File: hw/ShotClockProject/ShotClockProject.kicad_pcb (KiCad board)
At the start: 4 copper layers, 71.8 x 71.8 mm, 115 parts, among them IC1 TP4056-42-ESOP8_Rearanged, J1 USB4120-03-C_REVA, J2 Conn_ST_STDC14, J3 Conn_01x06_Pin, J4 SM03B-SRSS-TB(LF)(SN)(P), J5 Conn_01x02_Pin, J6 Conn_01x03_Pin, Q1 Q_NPN_BCE, Q2 Q_PMOS_SGD, Q3 Q_NPN_BCE, Q4 Q_NPN_BCE, SW1 TK-6580S-1, SW2 SW_SPDT, SW3 TK-6580S-2, SW4 TK-6580S-2, SW5 TK-6580S-2, U1 STM32F103RCT6, U2 LD39015M33R, U3 TPS63000, U4 TPS63000, U5 M74HC14YRM13TR, U6 USBLC6-2SC6, Y1 16MHz

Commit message: Finished routing
Added assembly holes
Added JLCJLCJLCJLC tag to hide their order number
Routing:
- net /Connectors to segment displays/DISP1_SEG_D: track 200.6 -> 244.8 mm, vias 5 -> 7
- net /Connectors to segment displays/DISP2_SEG_A: track 185.2 -> 226.8 mm, vias 5 -> 7
- net /Connectors to segment displays/DISP1_SEG_E: track 200.3 -> 240.1 mm, vias 5 -> 6
- net /Connectors to segment displays/DISP1_SEG_F: track 200.6 -> 239.9 mm, vias 5 -> 6
- net /Connectors to segment displays/DISP1_SEG_G: track 191.7 -> 227.1 mm, vias 7 -> 9
- net /Connectors to segment displays/DISP2_SEG_G: track 165.4 -> 192.3 mm, vias 5 -> 6
- net /Connectors to segment displays/DISP2_SEG_C: track 192.1 -> 218.3 mm, vias 7 -> 9
- net /Connectors to segment displays/DISP1_SEG_DP: track 198.9 -> 225.0 mm, vias 7 -> 9
- net /Connectors to segment displays/TIM2_CH1_PWM1_SEG: track 200.0 -> 224.8 mm, vias 7 -> 10
- net /Connectors to segment displays/DISP2_SEG_B: track 190.6 -> 215.3 mm, vias 5 -> 7
- net /Connectors to segment displays/DISP2_SEG_DP: track 144.6 -> 164.7 mm
- net /Connectors to segment displays/DISP2_SEG_F: track 174.3 -> 193.4 mm, vias 5 -> 6
- net /Connectors to segment displays/DISP2_SEG_E: track 173.3 -> 189.6 mm, vias 5 -> 6
- net GNDPWR: track 88.5 -> 92.1 mm
- net Net-(R1-Pad1): track 123.3 -> 121.9 mm
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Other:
- outline, holes or cut-outs redrawn
- board text added: "JLCJLCJLCJLC"

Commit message: Added LCSC Part number
Renamed output folders
Created first output files for REV1
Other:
- board text added: "REV 1"
- board text added: "Shot Clock Mainboard"
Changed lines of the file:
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@@
       (drillshape 0)
       (scaleselection 1)
-      (outputdirectory "output/mftr/gbr/v0.1/")
+      (outputdirectory "output/mftr/gerber/rev1/")
     )
   )
@@
     (fp_line (start 5.625 5) (end 4.625 5)
       (stroke (width 0.1) (type solid)) (layer "F.Fab"))
-    (pad "1" smd roundrect (at -7.65 -2.54 90) (size 4.6 1.1) (layers "F.Cu" "F.Paste" "F.Mask") (roundrect_rratio 0.227273)
+    (pad "1" smd roundrect (at -7.65 -2.54 90) (size 4.6 1.1) (layers "F.Cu" "F.Paste" "F.Mask") (roundrect_rratio 0.2272727273)
       (net 8 "+BATT") (pinfunction "S") (pintype "passive"))
-    (pad "2" smd roundrect (at -0.925 -2.775 90) (size 4.55 5.25) (layers "F.Cu" "F.Paste") (roundrect_rratio 0.054945)
+    (pad "2" smd roundrect (at -0.925 -2.775 90) (size 4.55 5.25) (layers "F.Cu" "F.Paste") (roundrect_rratio 0.05494505495)
       (net 90 "Net-(Q2-G)") (pinfunction "G") (pintype "input"))
-    (pad "2" smd roundrect (at -0.925 2.775 90) (size 4.55 5.25) (layers "F.Cu" "F.Paste") (roundrect_rratio 0.054945)
+    (pad "2" smd roundrect (at -0.925 2.775 90) (size 4.55 5.25) (layers "F.Cu" "F.Paste") (roundrect_rratio 0.05494505495)
       (net 90 "Net-(Q2-G)") (pinfunction "G") (pintype "input"))
-    (pad "2" smd roundrect (at 1.5 0 90) (size 9.4 10.8) (layers "F.Cu" "F.Mask") (roundrect_rratio 0.026596)
+    (pad "2" smd roundrect (at 1.5 0 90) (size 9.4 10.8) (layers "F.Cu" "F.Mask") (roundrect_rratio 0.02659595745)
       (net 90 "Net-(Q2-G)") (pinfunction "G") (pintype "input"))
-    (pad "2" smd roundrect (at 3.925 -2.775 90) (size 4.55 5.25) (layers "F.Cu" "F.Paste") (roundrect_rratio 0.054945)
+    (pad "2" smd roundrect (at 3.925 -2.775 90) (size 4.55 5.25) (layers "F.Cu" "F.Paste") (roundrect_rratio 0.05494505495)
       (net 90 "Net-(Q2-G)") (pinfunction "G") (pintype "input"))
-    (pad "2" smd roundrect (at 3.925 2.775 90) (size 4.55 5.25) (layers "F.Cu" "F.Paste") (roundrect_rratio 0.054945)
+    (pad "2" smd roundrect (at 3.925 2.775 90) (size 4.55 5.25) (layers "F.Cu" "F.Paste") (roundrect_rratio 0.05494505495)
       (net 90 "Net-(Q2-G)") (pinfunction "G") (pintype "input"))
-    (pad "3" smd roundrect (at -7.65 2.54 90) (size 4.6 1.1) (layers "F.Cu" "F.Paste" "F.Mask") (roundrect_rratio 0.227273)
+    (pad "3" smd roundrect (at -7.65 2.54 90) (size 4.6 1.1) (layers "F.Cu" "F.Paste" "F.Mask") (roundrect_rratio 0.2272727273)
       (net 44 "/Li-Po Battery and charger/charger_out") (pinfunction "D") (pintype "passive"))
     (model "${KICAD6_3DMODEL_DIR}/Package_TO_SOT_SMD.3dshapes/TO-263-2.wrl"
@@
     (property "Sheetname" "Connectors to segment displays")
     (attr smd)
-    (fp_text reference "FPC1" (at -7.75 3.25) (layer "F.SilkS")
+    (fp_text reference "FPC1" (at -9.6 -2 90) (layer "F.SilkS")
         (effects (font (size 1 1) (thickness 0.15)))
     )
@@
     (property "Sheetname" "STM32F103RCT6")
     (attr smd)
-    (fp_text reference "BUZZER1" (at 4.4 -5.4) (layer "F.SilkS")
+    (fp_text reference "BUZZER1" (at -6.2 1.2 90) (layer "F.SilkS")
         (effects (font (size 1 1) (thickness 0.15)))
     )
@@
   (gr_line (start 187 64.1) (end 121 64.1)
     (stroke (width 0.1) (type default)) (layer "Edge.Cuts"))
-  (gr_text "JLCJLCJLCJLC" (at 140 115.8) (layer "F.SilkS")
+  (gr_text "Shot \nClock \nMainboard" (at 123.8 135.2) (layer "F.SilkS")
+    (effects (font (size 1 1) (thickness 0.15)) (justify left bottom))
+  )
+  (gr_text "JLCJLCJLCJLC" (at 152.8 102) (layer "F.SilkS")
+    (effects (font (size 0.9 0.9) (thickness 0.15)) (justify left bottom))
+  )
+  (gr_text "REV 1" (at 120.4 129.8 90) (layer "F.SilkS")
     (effects (font (size 1 1) (thickness 0.15)) (justify left bottom))
   )

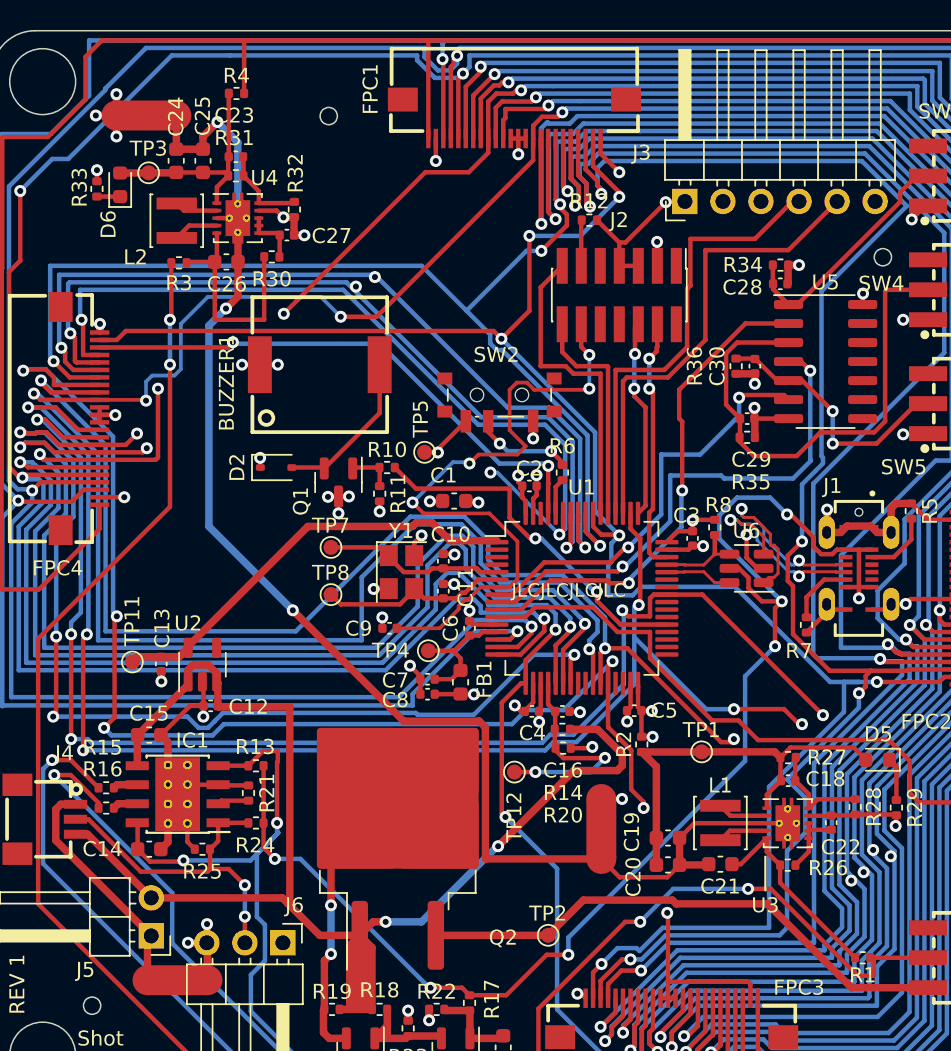
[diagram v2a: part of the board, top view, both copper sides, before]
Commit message: Added LCSC part numbers, and changed TPS vias
- Changed the footprint for the TPS regulators, so they don't have 0.2mm vias. Manually placed GND vias next to the footprint.
- Removed NETTIES to get rid of weird across the map connection of GND and GNDPWR.
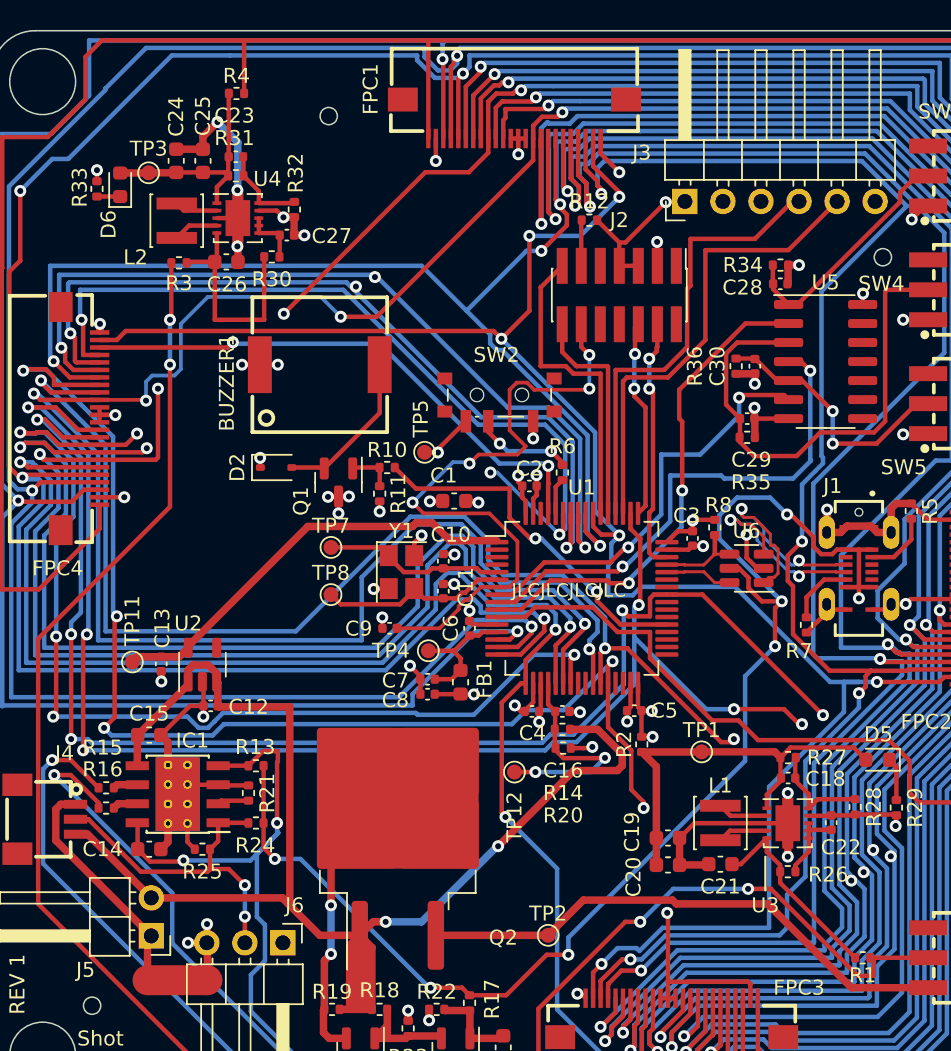
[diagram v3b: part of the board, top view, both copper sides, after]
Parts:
- removed NT2, NT3: NetTie_2, NetTie:NetTie-2_SMD_Pad2.0mm
- U3, U4: footprint Package_SON_Altered:Texas_DRC0010J_ThermalVias_Altered -> Package_SON:Texas_DRC0010J
- moved R26 0.44 mm to (171.2, 120.2)
- moved C18 0.17 mm to (171.3, 114.0)
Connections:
- C19 pad 2: GNDPWR -> GND
- C20 pad 2: GNDPWR -> GND
- C21 pad 2: GNDPWR -> GND
- C24 pad 2: GNDPWR -> GND
- C25 pad 2: GNDPWR -> GND
- C26 pad 2: GNDPWR -> GND
- U3 pad 11: GNDPWR -> GND
- U3 pad 3: GNDPWR -> GND
- U4 pad 11: GNDPWR -> GND
- U4 pad 3: GNDPWR -> GND
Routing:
- net GNDPWR: track 92.1 -> 0.00 mm, vias 3 -> 0
- net GND: track 161.9 -> 188.1 mm, vias 55 -> 56
- net /Connectors to segment displays/DISP2_SEG_B: track 215.3 -> 217.6 mm
- net /Connectors to segment displays/DISP2_SEG_DP: track 164.7 -> 163.7 mm

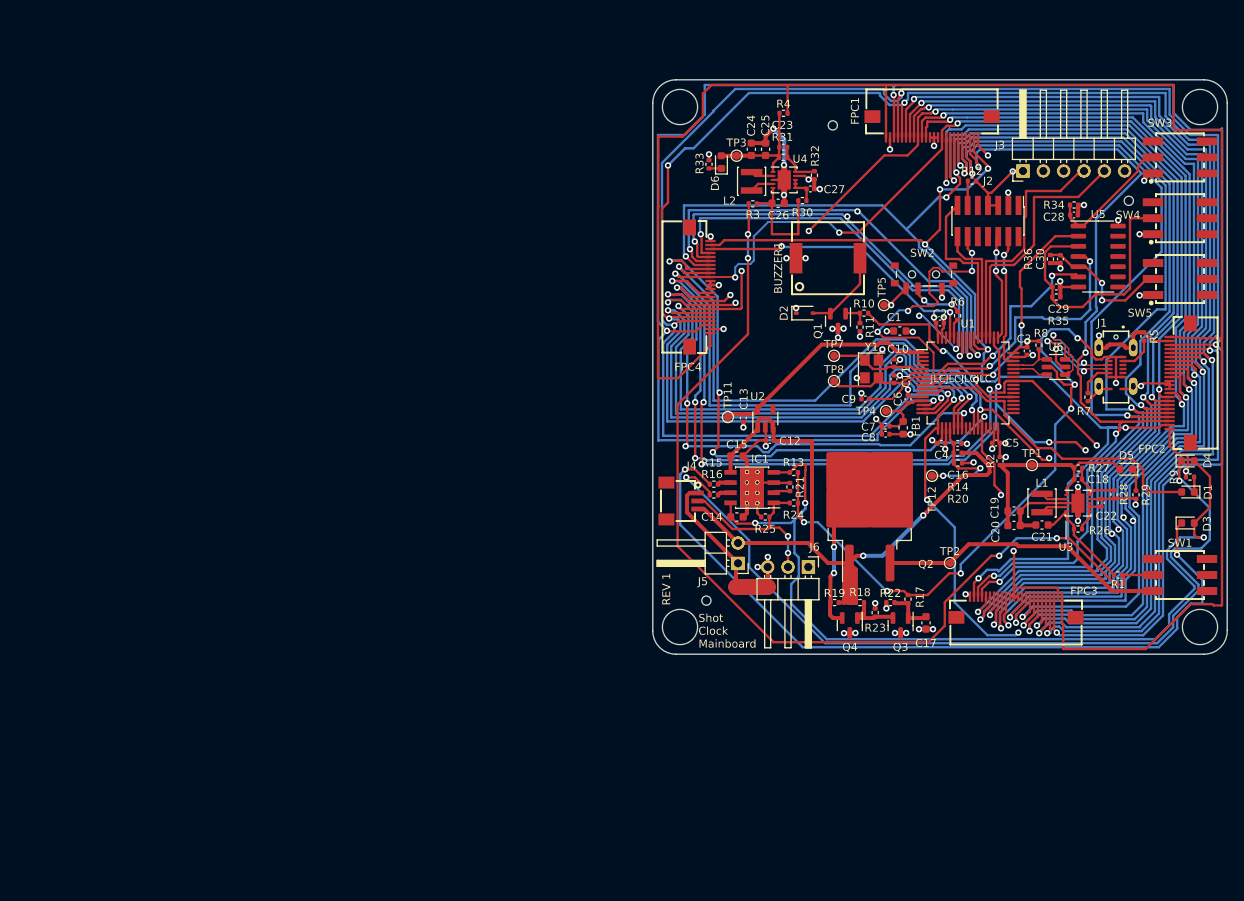
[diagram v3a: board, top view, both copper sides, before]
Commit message: Added I2C support
Calculated pull-up resistor values
Added 6 pin female headers to mainboard
Added nRESET line for the I2C chips
Removed PCB routing and part placement
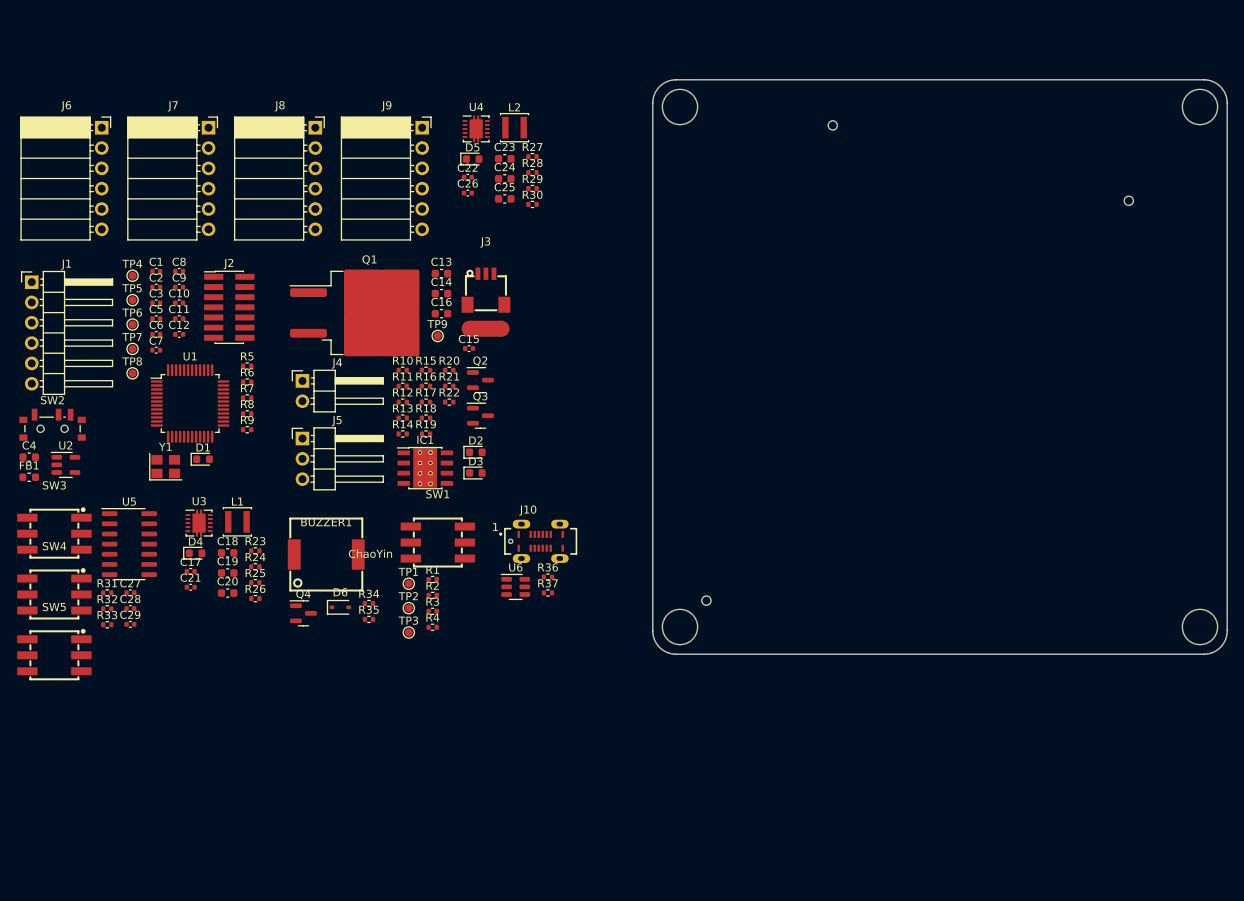
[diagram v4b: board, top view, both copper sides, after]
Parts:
- removed C30: 100n, Capacitor_SMD:C_0402_1005Metric
- removed FPC1, FPC2, FPC3, FPC4: AFC01-S24FCA-00, AFC01-S24FCA-00:FPC-SMD_P0.50-24P_FGS-XJ-H2.0
- removed TP11, TP12: TestPoint, TestPoint:TestPoint_Pad_D1.0mm
- added J10: USB4120-03-C_REVA, USB4120-03-C:GCT_USB4120-03-C_REVA_With3DModel, F.Cu at (104.1, 121.8)
- added J7: Conn_01x06_Pin, Connector_PinSocket_2.54mm:PinSocket_1x06_P2.54mm_Horizontal, F.Cu at (62.6, 70.1)
- added J8: Conn_01x06_Pin, Connector_PinSocket_2.54mm:PinSocket_1x06_P2.54mm_Horizontal, F.Cu at (75.9, 70.1)
- added J9: Conn_01x06_Pin, Connector_PinSocket_2.54mm:PinSocket_1x06_P2.54mm_Horizontal, F.Cu at (89.3, 70.1)
- added R37: 5k1, Resistor_SMD:R_0402_1005Metric, F.Cu at (105.0, 128.2)
- added TP6: TestPoint, TestPoint:TestPoint_Pad_D1.0mm, F.Cu at (53.1, 94.7)
- added TP9: TestPoint, TestPoint:TestPoint_Pad_D1.0mm, F.Cu at (91.2, 96.1)
- C1: value 10u -> 10n; footprint Capacitor_SMD:C_0603_1608Metric -> Capacitor_SMD:C_0402_1005Metric
- C10, C11: value 6p -> 100n
- C13: value 1u -> 10u; footprint Capacitor_SMD:C_0402_1005Metric -> Capacitor_SMD:C_0603_1608Metric
- C15: value 10u -> 100n; footprint Capacitor_SMD:C_0603_1608Metric -> Capacitor_SMD:C_0402_1005Metric
- C16: value 100n -> 10n; footprint Capacitor_SMD:C_0402_1005Metric -> Capacitor_SMD:C_0603_1608Metric
- C17: value 10n -> 2.2p; footprint Capacitor_SMD:C_0603_1608Metric -> Capacitor_SMD:C_0402_1005Metric
- C18, C23: value 2.2p -> 10u; footprint Capacitor_SMD:C_0402_1005Metric -> Capacitor_SMD:C_0603_1608Metric
- C2, C3, C9: value 100n -> 1u
- C21, C26: value 10u -> 0.1u; footprint Capacitor_SMD:C_0603_1608Metric -> Capacitor_SMD:C_0402_1005Metric
- C22: value 0.1u -> 2.2p
- C27: value 0.1u -> 100n
- C4: value 100n -> 4700n; footprint Capacitor_SMD:C_0402_1005Metric -> Capacitor_SMD:C_0603_1608Metric
- C6: value 10n -> 100n
- C7, C8: value 1u -> 6p
- D2: value 1N4148 -> G_LED; footprint Diode_SMD:D_SOD-323 -> LED_SMD:LED_0603_1608Metric
- D3: value G_LED -> R_LED
- D4: value R_LED -> G_LED
- D6: value G_LED -> 1N4148; footprint LED_SMD:LED_0603_1608Metric -> Diode_SMD:D_SOD-323
- J1: value USB4120-03-C_REVA -> Conn_01x06_Pin; footprint USB4120-03-C:GCT_USB4120-03-C_REVA_With3DModel -> Connector_PinHeader_2.54mm:PinHeader_1x06_P2.54mm_Horizontal
- J3: value Conn_01x06_Pin -> SM03B-SRSS-TB(LF)(SN)(P); footprint Connector_PinHeader_2.54mm:PinHeader_1x06_P2.54mm_Horizontal -> SM03B-SRSS-TB:CONN-SMD_SM03B-SRSS-TB-LF-SN-P
- J4: value SM03B-SRSS-TB(LF)(SN)(P) -> Conn_01x02_Pin; footprint SM03B-SRSS-TB:CONN-SMD_SM03B-SRSS-TB-LF-SN-P -> Connector_PinHeader_2.54mm:PinHeader_1x02_P2.54mm_Horizontal
- J5: value Conn_01x02_Pin -> Conn_01x03_Pin; footprint Connector_PinHeader_2.54mm:PinHeader_1x02_P2.54mm_Horizontal -> Connector_PinHeader_2.54mm:PinHeader_1x03_P2.54mm_Horizontal
- J6: value Conn_01x03_Pin -> Conn_01x06_Pin; footprint Connector_PinHeader_2.54mm:PinHeader_1x03_P2.54mm_Horizontal -> Connector_PinSocket_2.54mm:PinSocket_1x06_P2.54mm_Horizontal
- Q1: value Q_NPN_BCE -> Q_PMOS_SGD; footprint Package_TO_SOT_SMD:SOT-23 -> Package_TO_SOT_SMD:TO-263-2
- Q2: value Q_PMOS_SGD -> Q_NPN_BCE; footprint Package_TO_SOT_SMD:TO-263-2 -> Package_TO_SOT_SMD:SOT-23
- R10: value 300R -> 0.4R
- R11, R16, R17: value 1k -> 100k
- R12: value 100R -> 1k
- R13: value 0.4R -> 1k
- R14: value 1M -> 1k
- R18: value 1k -> 1k2
- R19: value 100k -> 10k
- R20, R31: value 1M -> 10k
- R21: value 1k2 -> 4780R
- R22: value 10k -> 86k6
- R23: value 10k -> 100R
- R24: value 4780R -> 1M
- R25: value 86k6 -> 178k
- R26, R30: value 100R -> 1k5
- R27: value 1M -> 100R
- R28: value 178k -> 1M
- R29: value 1k5 -> 110k
- R32: value 110k -> 10k
- R33, R8: value 1k5 -> 10k
- R34: value 10k -> 300R
- R35: value 10k -> 1k
- R36: value 10k -> 5k1
- R5: value 5k1 -> 1.5k
- R6: value 10k -> 1.5k
- R7: value 5k1 -> 130R
- R9: value 130R -> 100R
- U1: value STM32F103RCT6 -> STM32G070CBTx; footprint Package_QFP:LQFP-64_10x10mm_P0.5mm -> Package_QFP:LQFP-48_7x7mm_P0.5mm
- moved SW3 148.4 mm to (43.3, 120.8), turned to 0 degrees
- moved SW4 148.4 mm to (43.3, 128.4), turned to 0 degrees
- moved SW5 148.4 mm to (43.3, 136.0), turned to 0 degrees
- moved J1 135.9 mm to (40.5, 89.4), turned to 0 degrees
- moved C28 127.8 mm to (52.8, 130.2)
- moved U5 126.3 mm to (52.7, 122.1)
- moved D4 124.6 mm to (61.0, 123.3)
- moved C29 123.2 mm to (52.8, 132.2)
- moved D1 123.2 mm to (61.9, 111.5), turned to 0 degrees
- moved R9 118.0 mm to (67.4, 107.8)
- moved C4 114.0 mm to (40.1, 111.3), turned to 0 degrees
- moved R5 112.2 mm to (67.4, 99.9), turned to 0 degrees
- moved SW2 110.5 mm to (43.1, 107.4), turned to 0 degrees
- moved U3 109.9 mm to (61.4, 119.5)
- moved FB1 109.4 mm to (40.1, 113.8), turned to 0 degrees
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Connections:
- BUZZER1 pad 2: Net-(D2-A) -> Net-(D6-A)
- C1 pad 1: +3.3V -> +3.3VA
- C10 pad 1: /STM32F103RCT6/HSE_IN -> +BATT
- C11 pad 1: /STM32F103RCT6/HSE_OUT -> /STM32G070CBT6/VBAT
- C12 pad 1: +BATT -> /STM32G070CBT6/VBAT
- C13 pad 1: /STM32F103RCT6/VBAT -> Net-(D2-A)
- C14 pad 1: Net-(D3-A) -> +BATT
- C15 pad 1: +BATT -> /Li-Po Battery and charger/Batt_VoltageDivision_out
- C16 pad 1: /Li-Po Battery and charger/Batt_VoltageDivision_out -> Net-(Q2-B)
- C17 pad 1: Net-(Q3-B) -> /Voltage regulator 3v3/3v3_out
- C17 pad 2: GND -> Net-(U3-FB)
- C18 pad 2: Net-(U3-FB) -> GND
- C2 pad 1: +3.3V -> +3.3VA
- C20 pad 1: /Voltage regulator 3v3/3v3_out -> /Voltage regulator 3v3/batt_in
- C21 pad 1: /Voltage regulator 3v3/batt_in -> Net-(U3-EN)
- C22 pad 1: Net-(U3-EN) -> /Voltage regulator 5V/5v_out
- C22 pad 2: GND -> Net-(U4-FB)
- C23 pad 2: Net-(U4-FB) -> GND
- C25 pad 1: /Voltage regulator 5V/5v_out -> /Voltage regulator 5V/batt_in
- C26 pad 1: /Voltage regulator 5V/batt_in -> Net-(U4-EN)
- C27 pad 1: Net-(U4-EN) -> Net-(U5-1A)
- C28 pad 1: Net-(U5-1A) -> Net-(U5-2A)
- C29 pad 1: Net-(U5-2A) -> Net-(U5-3A)
- C6 pad 1: +3.3VA -> /STM32G070CBT6/NRST
- C7 pad 1: +3.3VA -> /STM32G070CBT6/HSE_IN
- C8 pad 1: +3.3V -> /STM32G070CBT6/HSE_OUT
- C9 pad 1: /STM32F103RCT6/NRST -> +BATT
- D1 pad 2: /STM32F103RCT6/ORANGE_LED -> /STM32G070CBT6/ORANGE_LED
- D2 pad 1: +3.3V -> Net-(D2-K)
- D3 pad 2: Net-(D3-A) -> Net-(D2-A)
- D4 pad 2: Net-(D3-A) -> /Voltage regulator 3v3/3v3_out
- D5 pad 2: /Voltage regulator 3v3/3v3_out -> /Voltage regulator 5V/5v_out
- D6 pad 1: Net-(D6-K) -> +3.3V
- D6 pad 2: /Voltage regulator 5V/5v_out -> Net-(D6-A)
- IC1 pad 4: Net-(D3-A) -> Net-(D2-A)
- IC1 pad 8: Net-(D3-A) -> Net-(D2-A)
- J2 pad 12: /STM32F103RCT6/NRST -> /STM32G070CBT6/NRST
- J2 pad 13: /STM32F103RCT6/UART5_RX -> /STM32G070CBT6/UART1_RX
- J2 pad 14: /STM32F103RCT6/UART5_TX -> /STM32G070CBT6/UART1_TX
- J2 pad 4: /STM32F103RCT6/SWDIO -> /STM32G070CBT6/SWDIO
- J2 pad 6: /STM32F103RCT6/SWCLK -> /STM32G070CBT6/SWCLK
- J3 pad 1: GND -> -BATT
- J3 pad 2: unconnected-(J3-Pin_2-Pad2) -> /Li-Po Battery and charger/IC_TEMP
- J3 pad 3: unconnected-(J3-Pin_3-Pad3) -> +BATT
- J3 pad 4: /STM32F103RCT6/UART4_RX -> unconnected-(J3-Pad4)
- J3 pad 5: /STM32F103RCT6/UART4_TX -> unconnected-(J3-Pad5)
- J4 pad 2: /Li-Po Battery and charger/IC_TEMP -> +BATT
- J5 pad 1: -BATT -> unconnected-(J5-Pin_1-Pad1)
- J5 pad 2: +BATT -> /Li-Po Battery and charger/IC_TEMP
- J6 pad 1: unconnected-(J6-Pin_1-Pad1) -> TLC59116_RESETn
- J6 pad 2: /Li-Po Battery and charger/IC_TEMP -> +3.3V
- J6 pad 3: GND -> +5V
- Q1 pad 1: Net-(Q1-B) -> +BATT
- Q1 pad 2: Net-(D2-A) -> Net-(Q1-G)
- Q1 pad 3: GND -> /Li-Po Battery and charger/charger_out
- Q2 pad 1: +BATT -> Net-(Q2-B)
- Q2 pad 2: Net-(Q2-G) -> Net-(Q2-C)
- Q2 pad 3: /Li-Po Battery and charger/charger_out -> GND
- Q3 pad 1: Net-(Q3-B) -> Net-(Q2-C)
- Q3 pad 2: Net-(Q3-C) -> Net-(Q1-G)
- Q4 pad 1: Net-(Q3-C) -> Net-(Q4-B)
- Q4 pad 2: Net-(Q2-G) -> Net-(D6-A)
- R10 pad 1: Net-(Q1-B) -> VBUS
- R10 pad 2: /STM32F103RCT6/PWM3_BUZZER -> Net-(D2-A)
- R11 pad 1: GND -> +BATT
- R11 pad 2: Net-(Q1-B) -> /Li-Po Battery and charger/Batt_VoltageDivision_out
- R12 pad 1: Net-(J2-GNDDetect) -> Net-(D2-K)
- R12 pad 2: GND -> /Li-Po Battery and charger/IC_STDBY_Green
- R13 pad 1: VBUS -> Net-(D3-K)
- R13 pad 2: Net-(D3-A) -> /Li-Po Battery and charger/IC_CHRG_Red
- R14 pad 1: +BATT -> Net-(Q2-B)
- R14 pad 2: /Li-Po Battery and charger/Batt_VoltageDivision_out -> VBUS
- R15 pad 1: Net-(D3-K) -> Net-(Q2-C)
- R15 pad 2: /Li-Po Battery and charger/IC_STDBY_Green -> +BATT
- R16 pad 1: Net-(D4-K) -> Net-(Q1-G)
- R16 pad 2: /Li-Po Battery and charger/IC_CHRG_Red -> +BATT
- R17 pad 1: Net-(Q3-B) -> /Li-Po Battery and charger/Batt_VoltageDivision_out
- R17 pad 2: VBUS -> GND
- R18 pad 1: Net-(Q3-C) -> GND
- R18 pad 2: +BATT -> /Li-Po Battery and charger/IC_PROG
- R19 pad 1: Net-(Q2-G) -> GND
- R19 pad 2: +BATT -> Net-(Q2-B)
- R20 pad 1: /Li-Po Battery and charger/Batt_VoltageDivision_out -> GND
- R20 pad 2: GND -> Net-(Q2-C)
- R21 pad 1: GND -> /Li-Po Battery and charger/IC_TEMP
- R21 pad 2: /Li-Po Battery and charger/IC_PROG -> VBUS
- R22 pad 2: Net-(Q3-B) -> /Li-Po Battery and charger/IC_TEMP
- R23 pad 1: GND -> /Voltage regulator 3v3/batt_in
- R23 pad 2: Net-(Q3-C) -> Net-(U3-EN)
- R24 pad 1: /Li-Po Battery and charger/IC_TEMP -> /Voltage regulator 3v3/3v3_out
- R24 pad 2: VBUS -> Net-(U3-FB)
- R25 pad 1: GND -> Net-(U3-FB)
- R25 pad 2: /Li-Po Battery and charger/IC_TEMP -> GND
- R26 pad 1: /Voltage regulator 3v3/batt_in -> Net-(D4-K)
- R26 pad 2: Net-(U3-EN) -> GND
- R27 pad 1: /Voltage regulator 3v3/3v3_out -> /Voltage regulator 5V/batt_in
- R27 pad 2: Net-(U3-FB) -> Net-(U4-EN)
- R28 pad 1: Net-(U3-FB) -> /Voltage regulator 5V/5v_out
- R28 pad 2: GND -> Net-(U4-FB)
- R29 pad 1: Net-(D5-K) -> Net-(U4-FB)
- R30 pad 1: /Voltage regulator 5V/batt_in -> Net-(D5-K)
- R30 pad 2: Net-(U4-EN) -> GND
- R31 pad 1: /Voltage regulator 5V/5v_out -> GND
- R31 pad 2: Net-(U4-FB) -> Net-(U5-1A)
- R32 pad 1: Net-(U4-FB) -> GND
- R32 pad 2: GND -> Net-(U5-2A)
- R33 pad 1: Net-(D6-K) -> GND
- R33 pad 2: GND -> Net-(U5-3A)
- R34 pad 1: GND -> Net-(Q4-B)
- R34 pad 2: Net-(U5-1A) -> /Buzzer_3v3_PWM/buzzer_pwm_in
- R35 pad 2: Net-(U5-2A) -> Net-(Q4-B)
- R36 pad 1: GND -> Net-(J10-CC1)
- R36 pad 2: Net-(U5-3A) -> GND
- R5 pad 1: Net-(J1-CC1) -> +3.3V
- R5 pad 2: GND -> I2C1_SCL
- R6 pad 1: /STM32F103RCT6/SW_BOOT0 -> +3.3V
- R6 pad 2: /STM32F103RCT6/BOOT0 -> I2C1_SDA
- R7 pad 1: Net-(J1-CC2) -> GND
- R7 pad 2: GND -> Net-(D1-K)
- R8 pad 1: +3.3V -> /STM32G070CBT6/SW_BOOT0
- R8 pad 2: /STM32F103RCT6/USB_D+ -> /STM32G070CBT6/BOOT0
- R9 pad 1: GND -> Net-(J2-GNDDetect)
- R9 pad 2: Net-(D1-K) -> GND
- SW2 pad 2: /STM32F103RCT6/SW_BOOT0 -> /STM32G070CBT6/SW_BOOT0
- TP7 pad 1: /STM32F103RCT6/HSE_IN -> /STM32G070CBT6/HSE_OUT
- TP8 pad 1: /STM32F103RCT6/HSE_OUT -> /STM32G070CBT6/VBAT
- U1 pad 1: /STM32F103RCT6/VBAT -> /STM32G070CBT6/BOOT0
- U1 pad 10: /STM32F103RCT6/button3_in -> /STM32G070CBT6/NRST
- U1 pad 11: /STM32F103RCT6/ORANGE_LED -> unconnected-(U1-PA0-Pad11)
- U1 pad 12: GND -> unconnected-(U1-PA1-Pad12)
- U1 pad 13: +3.3VA -> /STM32G070CBT6/UART2_TX
- U1 pad 14: /Connectors to segment displays/DISP1_SEG_A -> /STM32G070CBT6/UART2_RX
- U1 pad 15: /Connectors to segment displays/DISP1_SEG_B -> /STM32G070CBT6/button1_in
- U1 pad 16: /Connectors to segment displays/DISP1_SEG_C -> /STM32G070CBT6/button2_in
- U1 pad 17: /Connectors to segment displays/DISP1_SEG_D -> /STM32G070CBT6/button3_in
- U1 pad 18: GND -> unconnected-(U1-PA7-Pad18)
- U1 pad 19: +3.3V -> /STM32G070CBT6/ORANGE_LED
- U1 pad 20: /Li-Po Battery and charger/Batt_VoltageDivision_out -> unconnected-(U1-PB1-Pad20)
- U1 pad 21: /Connectors to segment displays/DISP1_SEG_E -> unconnected-(U1-PB2-Pad21)
- U1 pad 22: /Connectors to segment displays/DISP1_SEG_F -> unconnected-(U1-PB10-Pad22)
- U1 pad 23: /Connectors to segment displays/DISP1_SEG_G -> unconnected-(U1-PB11-Pad23)
- U1 pad 26: /Connectors to segment displays/DISP2_SEG_A -> unconnected-(U1-PB14-Pad26)
- U1 pad 27: /Connectors to segment displays/DISP2_SEG_B -> unconnected-(U1-PB15-Pad27)
- U1 pad 28: /Connectors to segment displays/DISP2_SEG_C -> unconnected-(U1-PA8-Pad28)
- U1 pad 31: GND -> TLC59116_RESETn
- U1 pad 32: +3.3V -> unconnected-(U1-PA10/NC-Pad32)
- U1 pad 33: unconnected-(U1-PB12-Pad33) -> I2C1_SCL
- U1 pad 34: unconnected-(U1-PB13-Pad34) -> I2C1_SDA
- U1 pad 37: /STM32F103RCT6/PWM3_BUZZER -> unconnected-(U1-PA15-Pad37)
- U1 pad 4: unconnected-(U1-PC15-Pad4) -> /STM32G070CBT6/VBAT
- U1 pad 41: /Connectors to segment displays/DISP1_SEG_DP -> unconnected-(U1-PD3-Pad41)
- U1 pad 42: unconnected-(U1-PA9-Pad42) -> /Buzzer_3v3_PWM/buzzer_pwm_in
- U1 pad 44: /STM32F103RCT6/USB_D- -> unconnected-(U1-PB5-Pad44)
- U1 pad 45: /STM32F103RCT6/USB_D+ -> /STM32G070CBT6/UART1_TX
- U1 pad 46: /STM32F103RCT6/SWDIO -> /STM32G070CBT6/UART1_RX
- U1 pad 47: GND -> unconnected-(U1-PB8-Pad47)
- U1 pad 48: +3.3V -> unconnected-(U1-PB9-Pad48)
- U1 pad 5: /STM32F103RCT6/HSE_IN -> +3.3VA
- U1 pad 6: /STM32F103RCT6/HSE_OUT -> +3.3V
- U1 pad 7: /STM32F103RCT6/NRST -> GND
- U1 pad 8: /STM32F103RCT6/button1_in -> /STM32G070CBT6/HSE_IN
- U1 pad 9: /STM32F103RCT6/button2_in -> /STM32G070CBT6/HSE_OUT
- U2 pad 5: /STM32F103RCT6/VBAT -> /STM32G070CBT6/VBAT
- U5 pad 2: /STM32F103RCT6/button3_in -> /STM32G070CBT6/button1_in
- U5 pad 4: /STM32F103RCT6/button2_in -> /STM32G070CBT6/button2_in
- U5 pad 6: /STM32F103RCT6/button1_in -> /STM32G070CBT6/button3_in
- U6 pad 1: /STM32F103RCT6/USB_CONN_D- -> /USB-C Connector/USB_CONN_D-
- U6 pad 3: /STM32F103RCT6/USB_CONN_D+ -> /USB-C Connector/USB_CONN_D+
- U6 pad 4: /STM32F103RCT6/USB_D+ -> GLOB_USB_D+
- U6 pad 6: /STM32F103RCT6/USB_D- -> GLOB_USB_D-
- Y1 pad 1: /STM32F103RCT6/HSE_IN -> /STM32G070CBT6/HSE_IN
- Y1 pad 3: /STM32F103RCT6/HSE_OUT -> /STM32G070CBT6/HSE_OUT
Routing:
- net /Connectors to segment displays/DISP1_SEG_A: track 262.0 -> 0.00 mm, vias 5 -> 0
- net /Connectors to segment displays/DISP1_SEG_B: track 258.7 -> 0.00 mm, vias 5 -> 0
- net /Connectors to segment displays/DISP1_SEG_C: track 256.8 -> 0.00 mm, vias 6 -> 0
- net /Connectors to segment displays/DISP1_SEG_D: track 244.8 -> 0.00 mm, vias 7 -> 0
- net /Connectors to segment displays/DISP1_SEG_E: track 240.1 -> 0.00 mm, vias 6 -> 0
- net /Connectors to segment displays/DISP1_SEG_F: track 239.9 -> 0.00 mm, vias 6 -> 0
- net /Connectors to segment displays/DISP1_SEG_G: track 227.1 -> 0.00 mm, vias 9 -> 0
- net /Connectors to segment displays/DISP2_SEG_A: track 226.8 -> 0.00 mm, vias 7 -> 0
- net +5V: track 225.2 -> 0.00 mm
- net /Connectors to segment displays/DISP1_SEG_DP: track 225.0 -> 0.00 mm, vias 9 -> 0
- net /Connectors to segment displays/TIM2_CH1_PWM1_SEG: track 224.8 -> 0.00 mm, vias 10 -> 0
- net /Connectors to segment displays/DISP2_SEG_C: track 218.3 -> 0.00 mm, vias 9 -> 0
- net /Connectors to segment displays/DISP2_SEG_B: track 217.6 -> 0.00 mm, vias 7 -> 0
- net /Connectors to segment displays/DISP2_SEG_F: track 193.4 -> 0.00 mm, vias 6 -> 0
- net /Connectors to segment displays/DISP2_SEG_G: track 192.3 -> 0.00 mm, vias 6 -> 0
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- removed copper zone on In2.Cu, net +3.3V
- removed copper zone on In1.Cu, net GND
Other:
- board text removed: "JLCJLCJLCJLC"
- board text removed: "REV 1"
- board text removed: "Shot Clock Mainboard"
